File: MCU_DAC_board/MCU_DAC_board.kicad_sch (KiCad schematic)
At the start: 15 parts, among them J1 Conn_01x08_Socket, J2 Conn_01x08_Socket, J3 Conn_01x08_Socket, J4 Conn_01x08_Socket, U1 ADAU1966AWBSTZ, U2 ESP32-WROOM 30-pin dev board

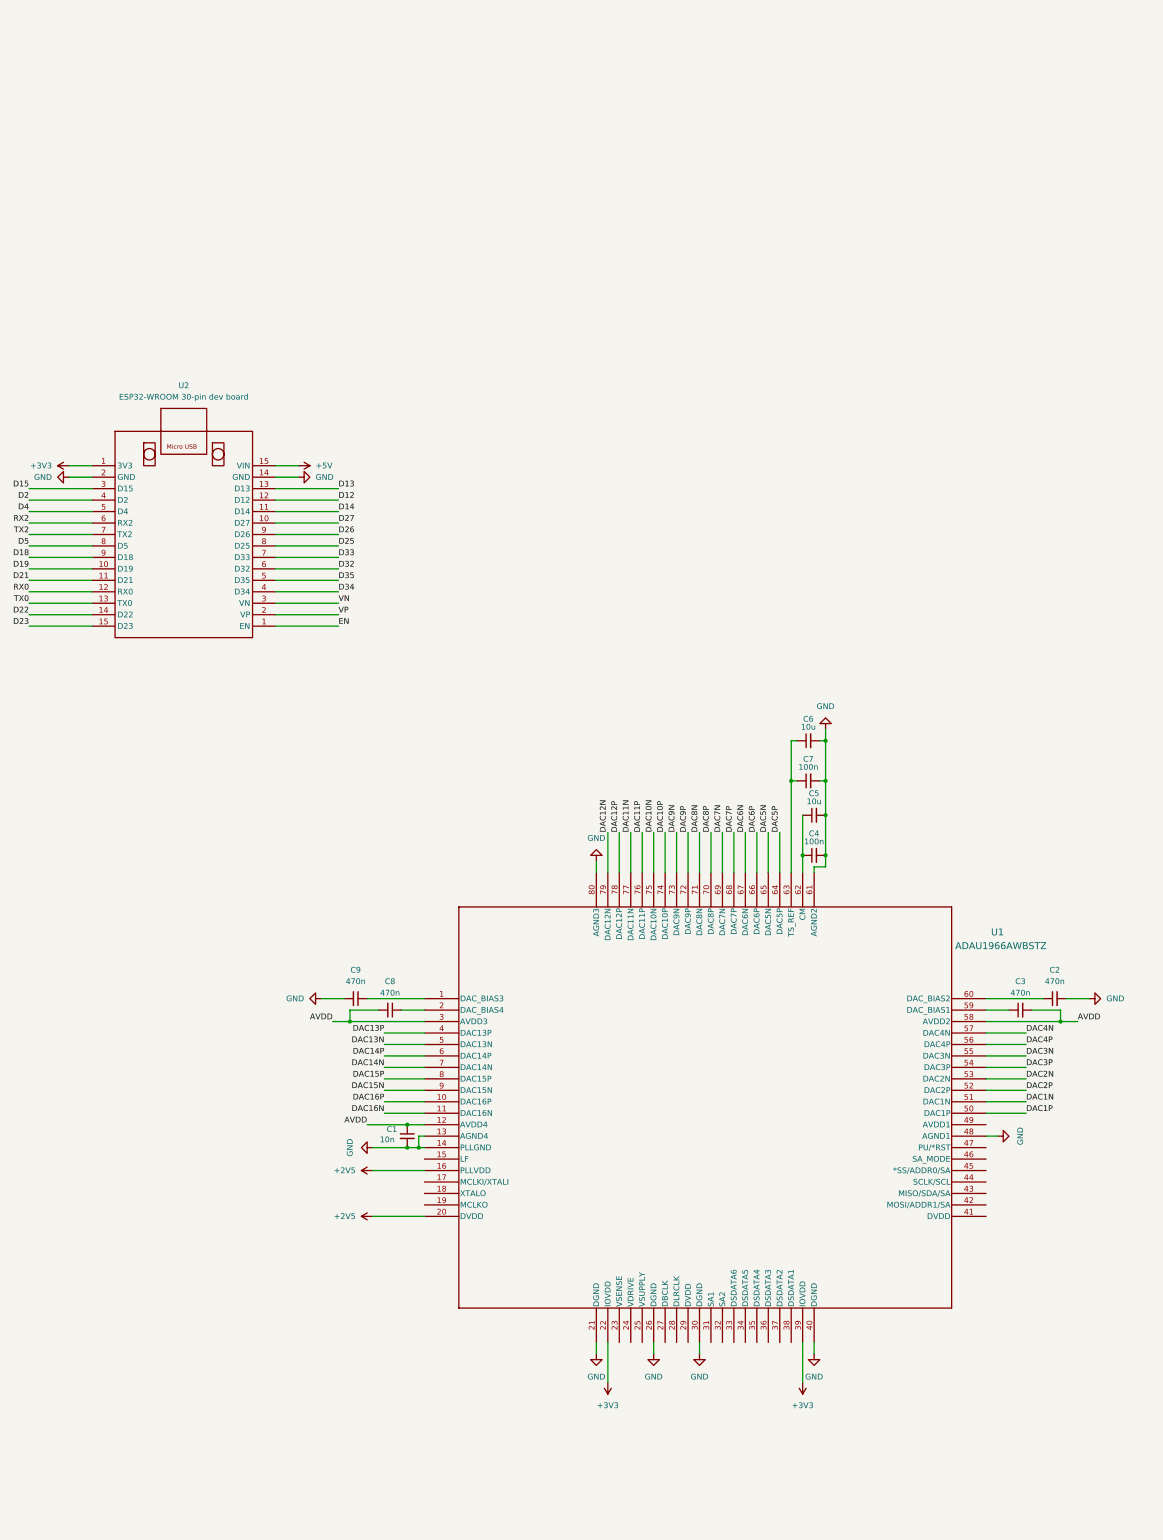
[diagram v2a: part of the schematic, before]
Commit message: Added 2.5V regulator circuit, jumpers on buffers
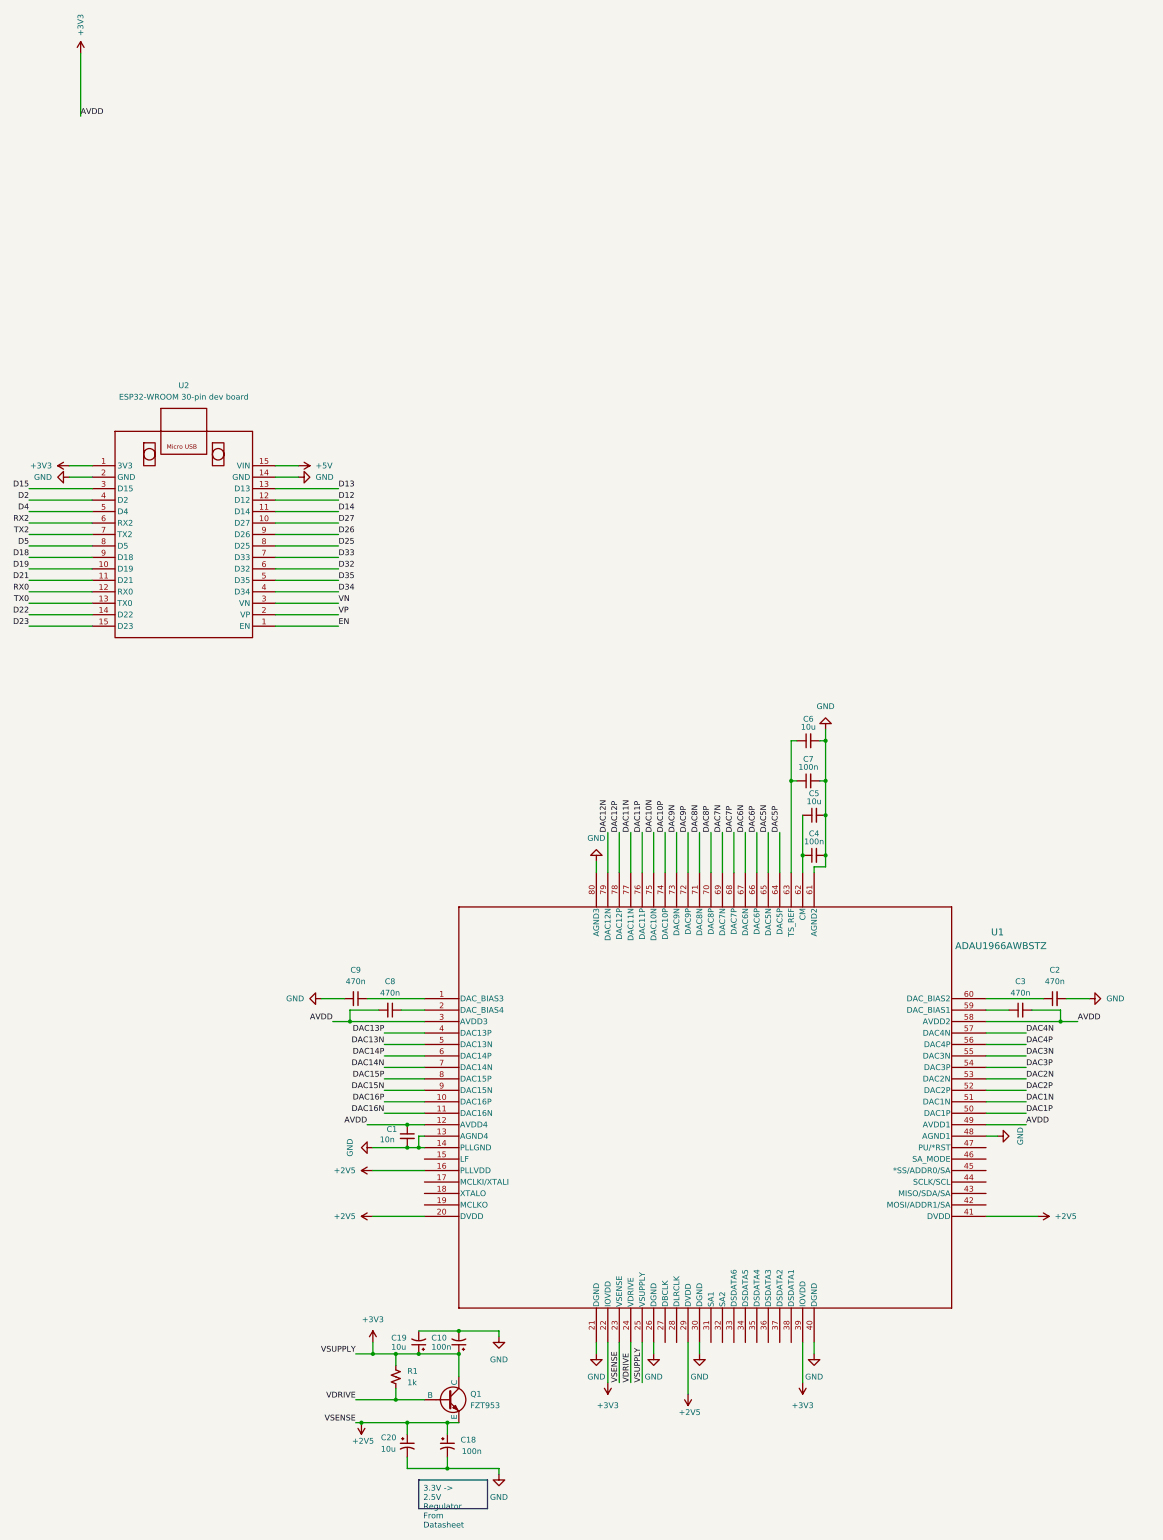
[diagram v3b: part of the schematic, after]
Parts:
- added C10, C18: 100n, symbol Device:C_Polarized_Small_US
- added C19, C20: 10u, symbol Device:C_Polarized_Small_US
- added Q1: FZT953, symbol Simulation_SPICE:NPN
- added R1: 1k, symbol Device:R_Small_US
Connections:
- net AVDD is gone; now on net +3V3: C1.1, C3.2, C8.2, U1.12 (AVDD4), U1.3 (AVDD3), U1.58 (AVDD2)
- net +2V5: now also U1.23 (VSENSE), U1.29 (DVDD), U1.41 (DVDD), C18.1, C20.1, Q1.3 (E)
- net +3V3: now also U1.25 (VSUPPLY), U1.49 (AVDD1), C10.1, C19.1, Q1.1 (C), R1.1
- net GND: now also C10.2, C18.2, C19.2, C20.2
- net VDRIVE: now reaches U1.24 (VDRIVE)
- net VDRIVE: now also Q1.2 (B), R1.2

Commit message: Added filtering between DAC and amp, power receptacles
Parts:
- added J10, J7, J8, J9: Screw_Terminal_01x02, symbol Connector:Screw_Terminal_01x02
- added J5, J6: Barrel_Jack, symbol Connector:Barrel_Jack
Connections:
- net +5V: now also J5.1
- net GND: now also J10.2 (Pin_2), J5.2, J6.2, J7.2 (Pin_2), J8.2 (Pin_2), J9.2 (Pin_2)
- net buffer1/Out1 renamed buffer1/Out1P
- net buffer1/Out2 renamed buffer1/Out1N
- net buffer1/Out3 renamed buffer1/Out2P
- net buffer1/Out4 renamed buffer1/Out2N
- net buffer2/Out1 renamed buffer2/Out1P
- net buffer2/Out2 renamed buffer2/Out1N
- net buffer2/Out3 renamed buffer2/Out2P
- net buffer2/Out4 renamed buffer2/Out2N
- net buffer3/Out1 renamed buffer3/Out1P
- net buffer3/Out2 renamed buffer3/Out1N
- net buffer3/Out3 renamed buffer3/Out2P
- net buffer3/Out4 renamed buffer3/Out2N
- net buffer4/Out1 renamed buffer4/Out1P
- net buffer4/Out2 renamed buffer4/Out1N
- net buffer4/Out3 renamed buffer4/Out2P
- net buffer4/Out4 renamed buffer4/Out2N
- net buffer5/Out1 renamed buffer5/Out1P
- net buffer5/Out2 renamed buffer5/Out1N
- net buffer5/Out3 renamed buffer5/Out2P
- net buffer5/Out4 renamed buffer5/Out2N
- net buffer6/Out1 renamed buffer6/Out1P
- net buffer6/Out2 renamed buffer6/Out1N
- net buffer6/Out3 renamed buffer6/Out2P
- net buffer6/Out4 renamed buffer6/Out2N
- net buffer7/Out1 renamed buffer7/Out1P
- net buffer7/Out2 renamed buffer7/Out1N
- net buffer7/Out3 renamed buffer7/Out2P
- net buffer7/Out4 renamed buffer7/Out2N
- net buffer8/Out1 renamed buffer8/Out1P
- net buffer8/Out2 renamed buffer8/Out1N
- net buffer8/Out3 renamed buffer8/Out2P
- net buffer8/Out4 renamed buffer8/Out2N
- new net +24V: J10.1 (Pin_1), J6.1, J7.1 (Pin_1), J8.1 (Pin_1), J9.1 (Pin_1)
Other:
- sheet buffer1 ports: added In1N, In1P, In2N, In2P, Out1N, Out1P, Out2N, Out2P; removed In1, In2, In3, In4, Out1, Out2, Out3, Out4
- sheet buffer2 ports: added In1N, In1P, In2N, In2P, Out1N, Out1P, Out2N, Out2P; removed In1, In2, In3, In4, Out1, Out2, Out3, Out4
- sheet buffer3 ports: added In1N, In1P, In2N, In2P, Out1N, Out1P, Out2N, Out2P; removed In1, In2, In3, In4, Out1, Out2, Out3, Out4
- sheet buffer4 ports: added In1N, In1P, In2N, In2P, Out1N, Out1P, Out2N, Out2P; removed In1, In2, In3, In4, Out1, Out2, Out3, Out4
- sheet buffer5 ports: added In1N, In1P, In2N, In2P, Out1N, Out1P, Out2N, Out2P; removed In1, In2, In3, In4, Out1, Out2, Out3, Out4
- sheet buffer6 ports: added In1N, In1P, In2N, In2P, Out1N, Out1P, Out2N, Out2P; removed In1, In2, In3, In4, Out1, Out2, Out3, Out4
- sheet buffer7 ports: added In1N, In1P, In2N, In2P, Out1N, Out1P, Out2N, Out2P; removed In1, In2, In3, In4, Out1, Out2, Out3, Out4
- sheet buffer8 ports: added In1N, In1P, In2N, In2P, Out1N, Out1P, Out2N, Out2P; removed In1, In2, In3, In4, Out1, Out2, Out3, Out4
- moved on the sheet: U2

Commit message: Removed buffers on DAC board
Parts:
- added C11, C12, C13, C14, C15, C16, C17, C21, C22, C23, C24, C25, C26, C27, C28, C29: 4n, symbol Device:C_Small
- added R10, R11, R12, R13, R14, R15, R16, R17, R18, R19, R2, R20, R21, R22, R23, R24, R25, R26, R27, R28, R29, R3, R30, R31, R32, R33, R4, R5, R6, R7, R8, R9: 500, symbol Device:R_Small_US
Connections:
- net DAC10N: now also R21.1
- net DAC10P: now also R20.1
- net DAC11N: now also R23.1
- net DAC11P: now also R22.1
- net DAC12N: now also R25.1
- net DAC12P: now also R24.1
- net DAC13N: now also R27.1
- net DAC13P: now also R26.1
- net DAC14N: now also R29.1
- net DAC14P: now also R28.1
- net DAC15N: now also R31.1
- net DAC15P: now also R30.1
- net DAC16N: now also R33.1
- net DAC16P: now also R32.1
- net DAC1N: now also R3.1
- net DAC1P: now also R2.1
- net DAC2N: now also R5.1
- net DAC2P: now also R4.1
- net DAC3N: now also R7.1
- net DAC3P: now also R6.1
- net DAC4N: now also R9.1
- net DAC4P: now also R8.1
- net DAC5N: now also R11.1
- net DAC5P: now also R10.1
- net DAC6N: now also R13.1
- net DAC6P: now also R12.1
- net DAC7N: now also R15.1
- net DAC7P: now also R14.1
- net DAC8N: now also R17.1
- net DAC8P: now also R16.1
- net DAC9N: now also R19.1
- net DAC9P: now also R18.1
- net buffer1/Out1N: no longer names the net of J1.2 (Pin_2)
- net buffer1/Out1N: now also C11.2, R3.2
- net buffer1/Out1P: no longer names the net of J1.1 (Pin_1)
- net buffer1/Out1P: now also C11.1, R2.2
- net buffer1/Out2N: no longer names the net of J1.4 (Pin_4)
- net buffer1/Out2N: now also C12.2, R5.2
- net buffer1/Out2P: no longer names the net of J1.3 (Pin_3)
- net buffer1/Out2P: now also C12.1, R4.2
- net buffer2/Out1N: no longer names the net of J1.6 (Pin_6)
- net buffer2/Out1N: now also C13.2, R7.2
- net buffer2/Out1P: no longer names the net of J1.5 (Pin_5)
- net buffer2/Out1P: now also C13.1, R6.2
- net buffer2/Out2N: no longer names the net of J1.8 (Pin_8)
- net buffer2/Out2N: now also C14.2, R9.2
- net buffer2/Out2P: no longer names the net of J1.7 (Pin_7)
- net buffer2/Out2P: now also C14.1, R8.2
- net buffer3/Out1N: no longer names the net of J2.2 (Pin_2)
- net buffer3/Out1N: now also C15.2, R11.2
- net buffer3/Out1P: no longer names the net of J2.1 (Pin_1)
- net buffer3/Out1P: now also C15.1, R10.2
- net buffer3/Out2N: no longer names the net of J2.4 (Pin_4)
- net buffer3/Out2N: now also C16.2, R13.2
- net buffer3/Out2P: no longer names the net of J2.3 (Pin_3)
- net buffer3/Out2P: now also C16.1, R12.2
- net buffer4/Out1N: no longer names the net of J2.6 (Pin_6)
- net buffer4/Out1N: now also C17.2, R15.2
- net buffer4/Out1P: no longer names the net of J2.5 (Pin_5)
- net buffer4/Out1P: now also C17.1, R14.2
- net buffer4/Out2N: no longer names the net of J2.8 (Pin_8)
- net buffer4/Out2N: now also C21.2, R17.2
- net buffer4/Out2P: no longer names the net of J2.7 (Pin_7)
- net buffer4/Out2P: now also C21.1, R16.2
- net buffer5/Out1N: no longer names the net of J3.2 (Pin_2)
- net buffer5/Out1N: now also C22.2, R19.2
- net buffer5/Out1P: no longer names the net of J3.1 (Pin_1)
- net buffer5/Out1P: now also C22.1, R18.2
- net buffer5/Out2N: no longer names the net of J3.4 (Pin_4)
- net buffer5/Out2N: now also C23.2, R21.2
- net buffer5/Out2P: no longer names the net of J3.3 (Pin_3)
- net buffer5/Out2P: now also C23.1, R20.2
- net buffer6/Out1N: no longer names the net of J3.6 (Pin_6)
- net buffer6/Out1N: now also C24.2, R23.2
- net buffer6/Out1P: no longer names the net of J3.5 (Pin_5)
- net buffer6/Out1P: now also C24.1, R22.2
- net buffer6/Out2N: no longer names the net of J3.8 (Pin_8)
- net buffer6/Out2N: now also C25.2, R25.2
- net buffer6/Out2P: no longer names the net of J3.7 (Pin_7)
- net buffer6/Out2P: now also C25.1, R24.2
- net buffer7/Out1N: no longer names the net of J4.2 (Pin_2)
- net buffer7/Out1N: now also C26.2, R27.2
- net buffer7/Out1P: no longer names the net of J4.1 (Pin_1)
- net buffer7/Out1P: now also C26.1, R26.2
- net buffer7/Out2N: no longer names the net of J4.4 (Pin_4)
- net buffer7/Out2N: now also C27.2, R29.2
- net buffer7/Out2P: no longer names the net of J4.3 (Pin_3)
- net buffer7/Out2P: now also C27.1, R28.2
- net buffer8/Out1N: no longer names the net of J4.6 (Pin_6)
- net buffer8/Out1N: now also C28.2, R31.2
- net buffer8/Out1P: no longer names the net of J4.5 (Pin_5)
- net buffer8/Out1P: now also C28.1, R30.2
- net buffer8/Out2N: no longer names the net of J4.8 (Pin_8)
- net buffer8/Out2N: now also C29.2, R33.2
- net buffer8/Out2P: no longer names the net of J4.7 (Pin_7)
- net buffer8/Out2P: now also C29.1, R32.2
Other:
- removed sheet buffer1
- removed sheet buffer2
- removed sheet buffer3
- removed sheet buffer4
- removed sheet buffer5
- removed sheet buffer6
- removed sheet buffer7
- removed sheet buffer8
- moved on the sheet: C1, C10, C18, C19, C2, C20, C3, C4, C5, C6, C7, C8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
